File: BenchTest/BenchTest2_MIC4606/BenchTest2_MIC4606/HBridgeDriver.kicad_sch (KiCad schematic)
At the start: 39 parts, among them J1 Conn_01x01_Socket, J2 Conn_01x01_Socket, J3 Conn_01x01_Socket, J4 Conn_01x01_Socket, J5 Conn_01x01_Socket, J6 Conn_01x01_Socket, J7 Conn_01x01_Socket, J8 Conn_01x01_Socket

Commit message: WIP New Motor Design
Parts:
- removed C1: 0.1u, Capacitor_SMD:C_0402_1005Metric_Pad0.74x0.62mm_HandSolder, symbol Device:C
- removed C2: 1u, Capacitor_SMD:C_0603_1608Metric_Pad1.08x0.95mm_HandSolder, symbol Device:C
- removed C3: 2.2u, Capacitor_SMD:C_0603_1608Metric_Pad1.08x0.95mm_HandSolder, symbol Device:C
- removed C4, C5, C8, C9: 4.7n, Capacitor_SMD:C_0805_2012Metric_Pad1.18x1.45mm_HandSolder, symbol Device:C
- removed C6, C7: 10u, Capacitor_SMD:C_0805_2012Metric_Pad1.18x1.45mm_HandSolder, symbol Device:C
- removed D1, D2, D3, D4, D5, D6: D, Diode_SMD:D_SOD-123F, symbol Device:D
- removed J1, J2, J3, J4, J5, J6, J7, J8: Conn_01x01_Socket, Connector_PinHeader_2.54mm:PinHeader_1x01_P2.54mm_Vertical, symbol Connector:Conn_01x01_Socket
- removed R1: 100k, Resistor_SMD:R_0402_1005Metric_Pad0.72x0.64mm_HandSolder, symbol Device:R
- removed R10, R2, R5, R9: 6.8, Resistor_SMD:R_0805_2012Metric_Pad1.20x1.40mm_HandSolder, symbol Device:R
- removed R11, R3, R4, R8: 18, Resistor_SMD:R_0805_2012Metric_Pad1.20x1.40mm_HandSolder, symbol Device:R
- removed R6, R7: 3.3, Resistor_SMD:R_0805_2012Metric_Pad1.20x1.40mm_HandSolder, symbol Device:R
- removed TP1, TP2, TP3, TP4: TestPoint, TestPoint:TestPoint_Pad_1.0x1.0mm, symbol Connector:TestPoint
- removed U1: ~, Package_SO:TSSOP-16_4.4x5mm_P0.65mm, symbol New_Library:MIC4606

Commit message: H Bridge Continuation
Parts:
- added C1, C2, C3, C8: 0.1u, Capacitor_SMD:C_0402_1005Metric_Pad0.74x0.62mm_HandSolder, symbol Device:C
- added C10, C11, C14, C15, C16, C17, C18, C19, C9: C, symbol Device:C
- added D10, D7, D8, D9: D_Schottky, symbol Device:D_Schottky
- added D11: D, symbol Device:D
- added D12, D13: SMAJ120CA, Diode_SMD:D_SMA, symbol Diode:SMAJ120CA
- added J5, J6: Conn_01x01_Socket, symbol Connector:Conn_01x01_Socket
- added Q5, Q6: Q_NMOS_DGS, symbol Transistor_FET:Q_NMOS_DGS
- added Q7, Q8: Q_PMOS_DGS, symbol Transistor_FET:Q_PMOS_DGS
- added R10, R11, R13, R9: 33, Resistor_SMD:R_0402_1005Metric_Pad0.72x0.64mm_HandSolder, symbol Device:R
- added R15, R16, R18, R19, R20, R21, R22, R23: R, symbol Device:R
- added R17: 0, symbol Device:R
- added U10, U3: ~, Package_SO:SOIC-8_3.9x4.9mm_P1.27mm, symbol New_Library:FAN3217
- added U6, U7, U8, U9: TLP2767, Package_SO:SO-6L_10x3.84mm_P1.27mm, symbol Isolator:TLP2767
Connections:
- new net: R20.2, U8.1 (A)
- new net: D10.2 (A), Q6.2 (G), R13.2
- new net: D9.2 (A), Q8.2 (G), R11.2
- new net: R18.2, U7.1 (A)
- new net: D8.2 (A), Q7.2 (G), R10.2
- new net: R15.2, U6.1 (A)
- new net: D7.2 (A), Q5.2 (G), R9.2
- new net: R21.2, U9.1 (A)
- new net F1: D12.2 (A2), J5.1 (Pin_1), Q5.1 (D), Q7.3 (S)
- new net F2: D13.2 (A2), J6.1 (Pin_1), Q6.1 (D), Q8.3 (S)
- new net G+_1: D8.1 (K), R10.1, U3.7 (OUTA)
- new net G+_2: D9.1 (K), R11.1, U10.7 (OUTA)
- new net G-_1: D7.1 (K), R9.1, U3.5 (OUTB)
- new net G-_2: D10.1 (K), R13.1, U10.5 (OUTB)
- new net GND: C1.2, C2.2, C3.2, C8.2, U10.3 (GND), U3.3 (GND), U6.3 (K), U6.4 (GND), U7.3 (K), U7.4 (GND), U8.3 (K), U8.4 (GND), U9.3 (K), U9.4 (GND)
- new net IN1+: R15.1, R16.1
- new net IN1-: R18.1, R19.1
- new net IN2+: R20.1, R23.1
- new net IN2-: R21.1, R22.1
- new net INA1: R16.2, U10.2 (INA), U3.2 (INA), U6.5 (VO), U8.5 (VO)
- new net INA2: R23.2
- new net INB1: R19.2, U3.4 (INB), U7.5 (VO)
- new net INB2: R22.2, U10.4 (INB), U9.5 (VO)
- new net VBAT+: C10.1, C11.1, C14.1, C15.1, C16.1, C17.1, C18.1, C19.1, C9.1, Q7.1 (D), Q8.1 (D)
- new net VBAT-: C10.2, C11.2, C14.2, C15.2, C16.2, C17.2, C18.2, C19.2, C9.2, D12.1 (A1), D13.1 (A1), Q5.3 (S), Q6.3 (S)
- new net Vdrive: D11.2 (A), R17.1
- new net Vdrive_iso: C1.1, C2.1, C3.1, C8.1, D11.1 (K), R17.2, U10.6 (VDD), U3.6 (VDD), U6.6 (VDD), U7.6 (VDD), U8.6 (VDD), U9.6 (VDD)
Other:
- note added: "Cap Bank Effective Capacitance: TODO"
- note added: "TODO investigate this"
- note added: "TODO why TVS? TODO What voltage? > vbat?"

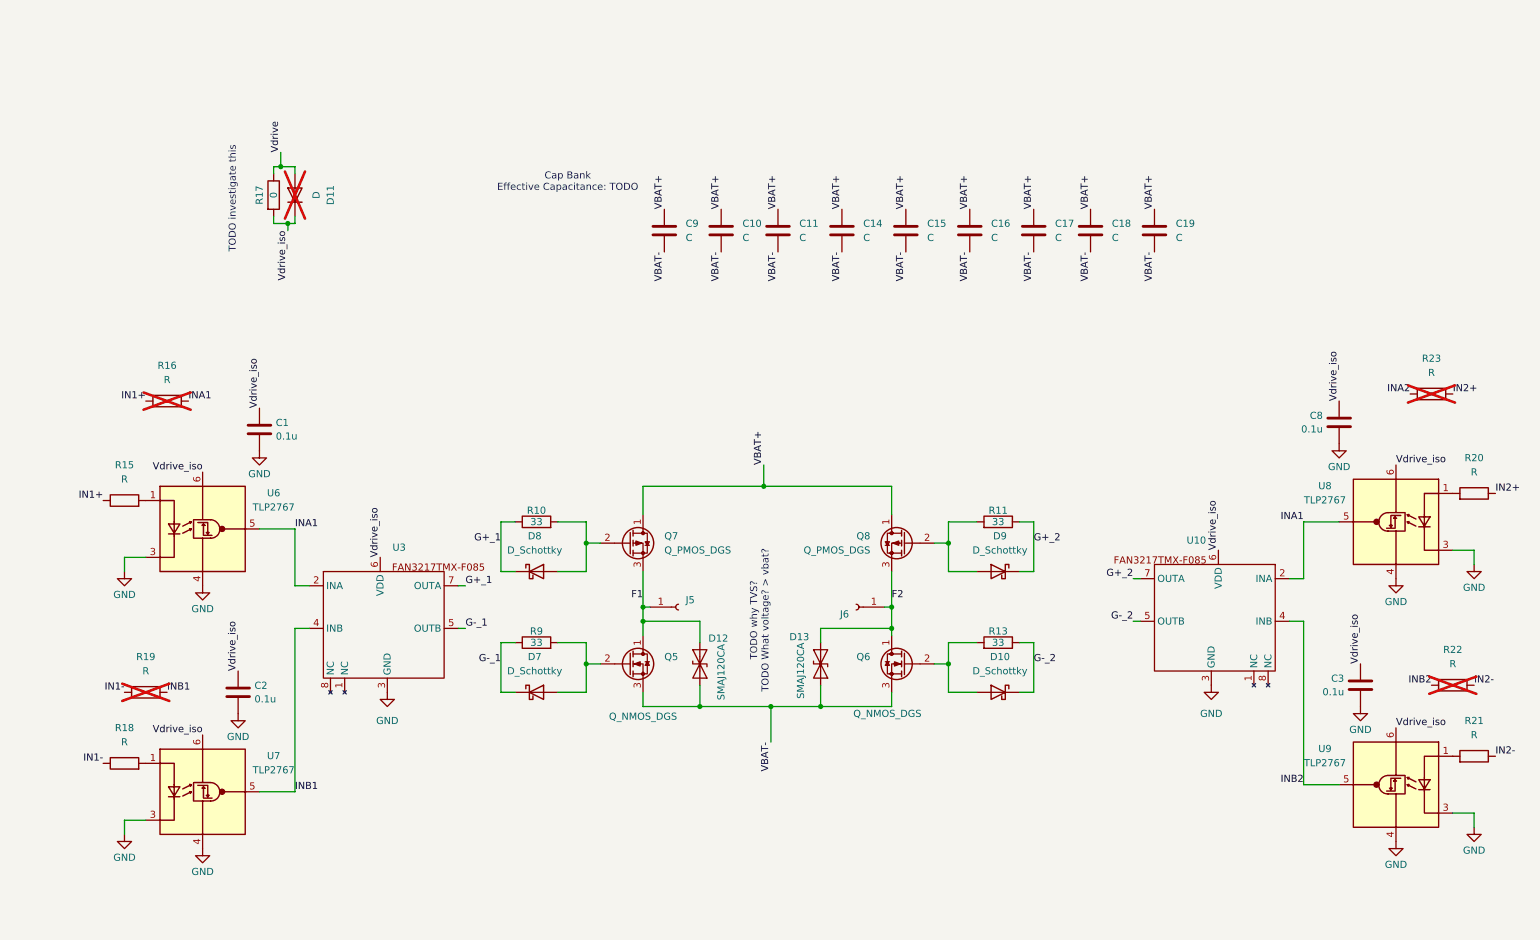
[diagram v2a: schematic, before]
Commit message: Defined Some parts, added notes for Arm/regen/H bridge
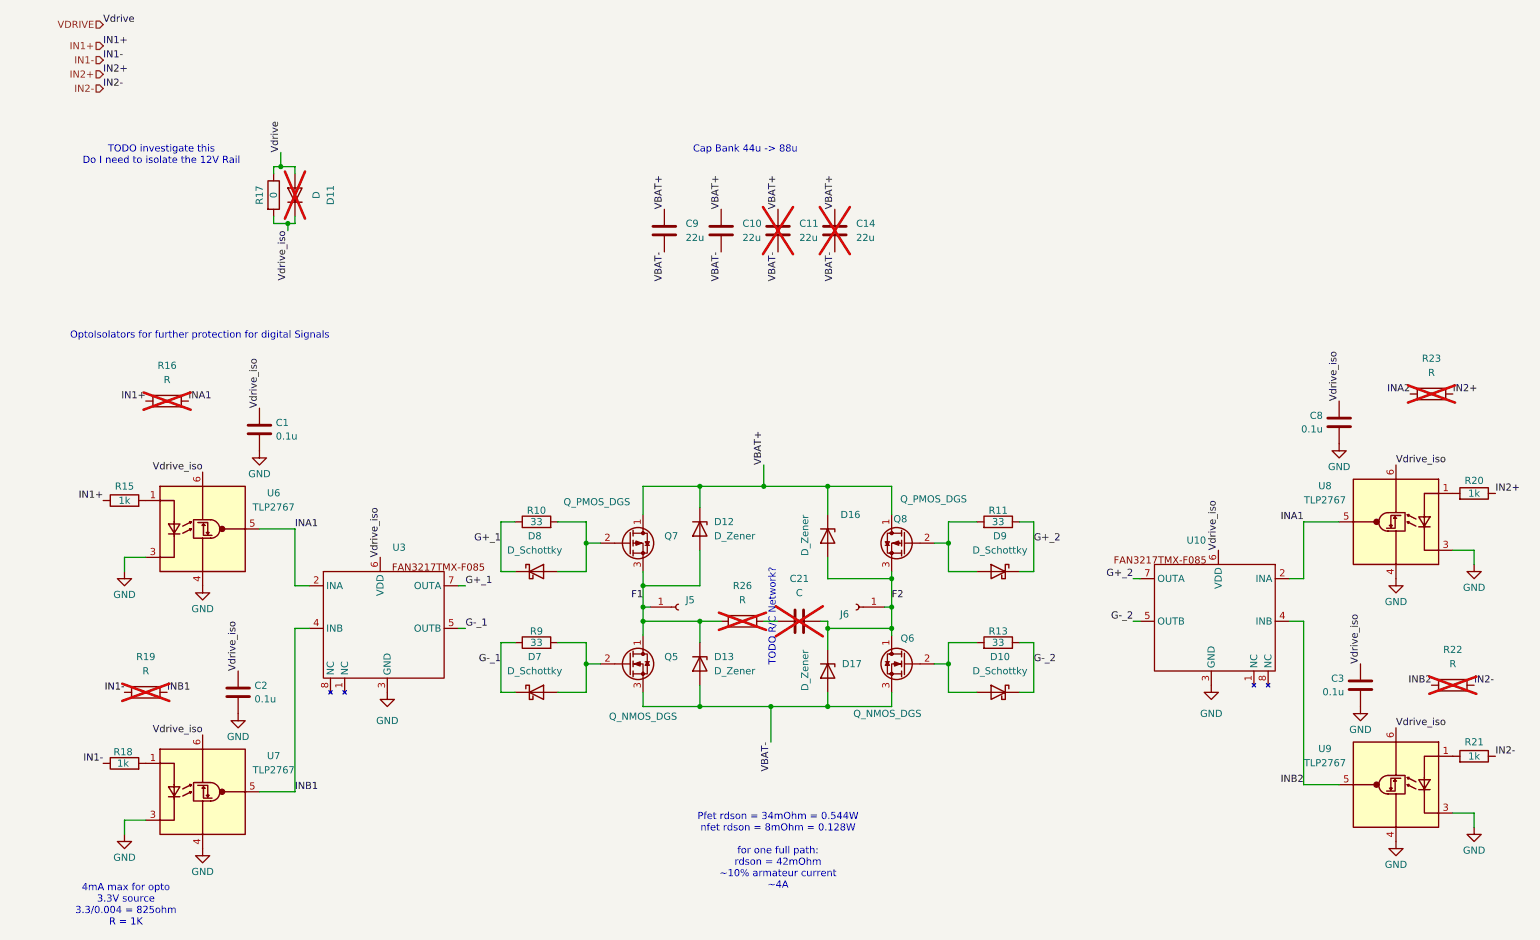
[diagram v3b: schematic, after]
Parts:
- removed C15, C16, C17, C18, C19: C, symbol Device:C
- removed D12, D13: SMAJ120CA, Diode_SMD:D_SMA, symbol Diode:SMAJ120CA
- added C21: C, Capacitor_SMD:C_1206_3216Metric_Pad1.33x1.80mm_HandSolder, symbol Device:C
- added D12, D13, D16, D17: D_Zener, Diode_SMD:D_SMC, symbol Device:D_Zener
- added R26: R, Resistor_SMD:R_1206_3216Metric_Pad1.30x1.75mm_HandSolder, symbol Device:R
- C10, C9: value C -> 22u; P/N (none) -> 226AVG100MFBJ
- C11, C14: value C -> 22u; P/N (none) -> 226AVG100MFBJ; now not fitted
- R15, R18, R20, R21: value R -> 1k
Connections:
- net F1: now also D12.2 (A), D13.1 (K), R26.1
- net F2: now also C21.2, D16.2 (A), D17.1 (K)
- net VBAT+: now also D12.1 (K), D16.1 (K)
- net VBAT-: now also D13.2 (A), D17.2 (A)
- net Vdrive renamed VDRIVE
- new net: C21.1, R26.2
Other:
- note added: "4mA max for opto 3.3V source 3.3/0.004 = 825ohm R = 1K"
- note added: "Cap Bank 44u -> 88u"
- note added: "OptoIsolators for further protection for digital Signals"
- note added: "Pfet rdson = 34mOhm = 0.544W nfet rdson = 8mOhm = 0.128W for one full path: rdson = 42mOhm ~10% armateur current ~4A"
- note added: "TODO R/C Network?"
- note added: "TODO investigate this Do I need to isolate the 12V Rail"
- note removed: "Cap Bank Effective Capacitance: TODO"
- note removed: "TODO investigate this"
- note removed: "TODO why TVS? TODO What voltage? > vbat?"

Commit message: Additional Documents / Routing
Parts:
- removed J5, J6: Conn_01x01_Socket, symbol Connector:Conn_01x01_Socket
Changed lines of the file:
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@@
 		)
 	)
-	(label "F1"
-		(at 118.11 119.38 180)
-		(effects
-			(font
-				(size 1.27 1.27)
-			)
-			(justify right bottom)
-		)
-	)
 	(label "IN1+"
 		(at 21.59 101.6 180)
@@
 		)
 	)
+	(label "F1"
+		(at 21.59 33.02 0)
+		(effects
+			(font
+				(size 1.27 1.27)
+			)
+			(justify left bottom)
+		)
+	)
 	(label "INB1"
 		(at 55.88 153.67 0)
@@
 		)
 	)
+	(label "F2"
+		(at 161.29 120.65 180)
+		(effects
+			(font
+				(size 1.27 1.27)
+			)
+			(justify right bottom)
+		)
+	)
 	(label "VBAT+"
 		(at 121.92 49.53 90)
@@
 		)
 	)
+	(label "F2"
+		(at 21.59 35.56 0)
+		(effects
+			(font
+				(size 1.27 1.27)
+			)
+			(justify left bottom)
+		)
+	)
 	(label "VBAT-"
 		(at 140.97 144.78 270)
@@
 		)
 	)
-	(label "F2"
-		(at 162.56 119.38 0)
-		(effects
-			(font
-				(size 1.27 1.27)
-			)
-			(justify left bottom)
-		)
-	)
 	(label "G-_2"
 		(at 187.96 130.81 0)
@@
 		)
 	)
+	(label "F1"
+		(at 119.38 120.65 0)
+		(effects
+			(font
+				(size 1.27 1.27)
+			)
+			(justify left bottom)
+		)
+	)
 	(hierarchical_label "IN1+"
 		(shape input)
@@
 		)
 	)
+	(hierarchical_label "F2"
+		(shape input)
+		(at 21.59 35.56 180)
+		(effects
+			(font
+				(size 1.27 1.27)
+			)
+			(justify right)
+		)
+	)
+	(hierarchical_label "F1"
+		(shape input)
+		(at 21.59 33.02 180)
+		(effects
+			(font
+				(size 1.27 1.27)
+			)
+			(justify right)
+		)
+	)
 	(hierarchical_label "IN2+"
 		(shape input)
@@
 	)
 	(symbol
-		(lib_id "Connector:Conn_01x01_Socket")
-		(at 156.21 120.65 180)
-		(unit 1)
-		(exclude_from_sim no)
-		(in_bom yes)
-		(on_board yes)
-		(dnp no)
-		(property "Reference" "J6"
-			(at 154.94 121.9201 0)
-			(effects
-				(font
-					(size 1.27 1.27)
-				)
-				(justify left)
-			)
-		)
-		(property "Value" "Conn_01x01_Socket"
-			(at 159.766 117.094 0)
-			(effects
-				(font
-					(size 1.27 1.27)
-				)
-				(justify left)
-				(hide yes)
-			)
-		)
-		(property "Footprint" ""
-			(at 156.21 120.65 0)
-			(effects
-				(font
-					(size 1.27 1.27)
-				)
-				(hide yes)
-			)
-		)
-		(property "Datasheet" "~"
-			(at 156.21 120.65 0)
-			(effects
-				(font
-					(size 1.27 1.27)
-				)
-				(hide yes)
-			)
-		)
-		(property "Description" "Generic connector, single row, 01x01, script generated"
-			(at 156.21 120.65 0)
-			(effects
-				(font
-					(size 1.27 1.27)
-				)
-				(hide yes)
-			)
-		)
-		(pin "1"
-		)
-		(instances
-			(project "BenchTest2_MIC4606"
-				(path "/5c5197d3-4aa5-4f8b-b790-1e4b8d49fd62/ca249708-ec09-41b0-b71d-70bebe19cbfd"
-					(reference "J6")
-					(unit 1)
-				)
-			)
-		)
-	)
-	(symbol
 		(lib_id "Device:C")
 		(at 132.08 53.34 0)
@@
 					(unit 1)
 				)
-			)
-		)
-	)
-	(symbol
-		(lib_id "Connector:Conn_01x01_Socket")
-		(at 124.46 120.65 0)
-		(unit 1)
-		(exclude_from_sim no)
-		(in_bom yes)
-		(on_board yes)
-		(dnp no)
-		(property "Reference" "J5"
-			(at 125.73 119.3799 0)
-			(effects
-				(font
-					(size 1.27 1.27)
-				)
-				(justify left)
-			)
-		)
-		(property "Value" "Conn_01x01_Socket"
-			(at 120.904 124.206 0)
-			(effects
-				(font
-					(size 1.27 1.27)
-				)
-				(justify left)
-				(hide yes)
-			)
-		)
-		(property "Footprint" ""
-			(at 124.46 120.65 0)
-			(effects
-				(font
-					(size 1.27 1.27)
-				)
-				(hide yes)
-			)
-		)
-		(property "Datasheet" "~"
-			(at 124.46 120.65 0)
-			(effects
-				(font
-					(size 1.27 1.27)
-				)
-				(hide yes)
-			)
-		)
-		(property "Description" "Generic connector, single row, 01x01, script generated"
-			(at 124.46 120.65 0)
-			(effects
-				(font
-					(size 1.27 1.27)
-				)
-				(hide yes)
-			)
-		)
-		(pin "1"
-		)
-		(instances
-			(project ""
-				(path "/5c5197d3-4aa5-4f8b-b790-1e4b8d49fd62/ca249708-ec09-41b0-b71d-70bebe19cbfd"
-					(reference "J5")
-					(unit 1)
-				)

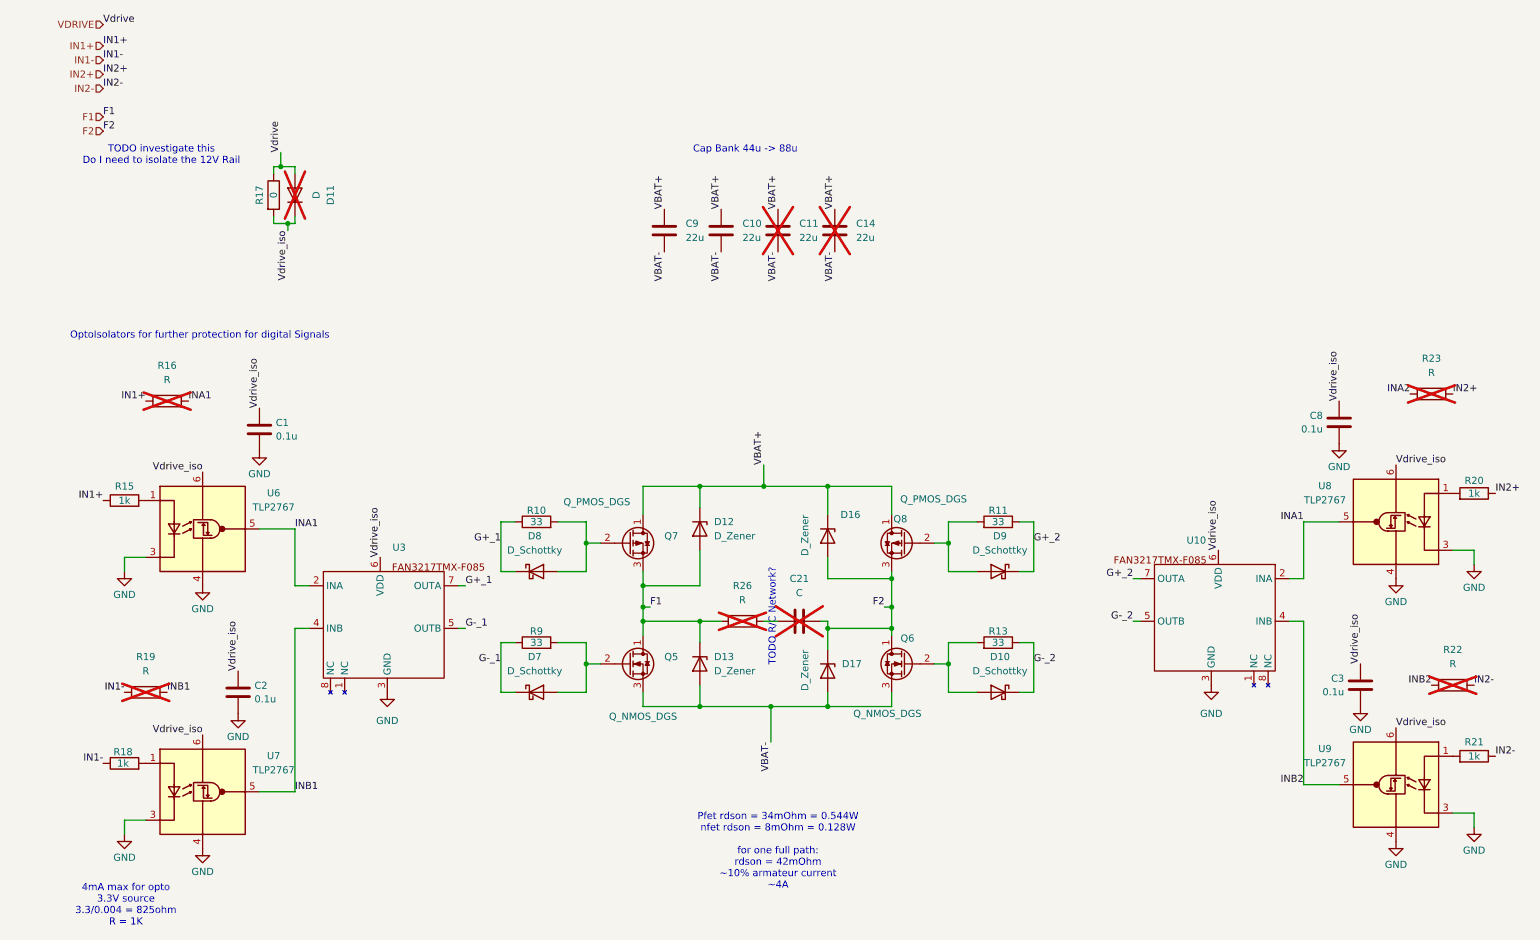
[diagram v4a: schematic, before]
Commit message: Removed Optoisolators from digital Signals
Will be requiring these on the drive side
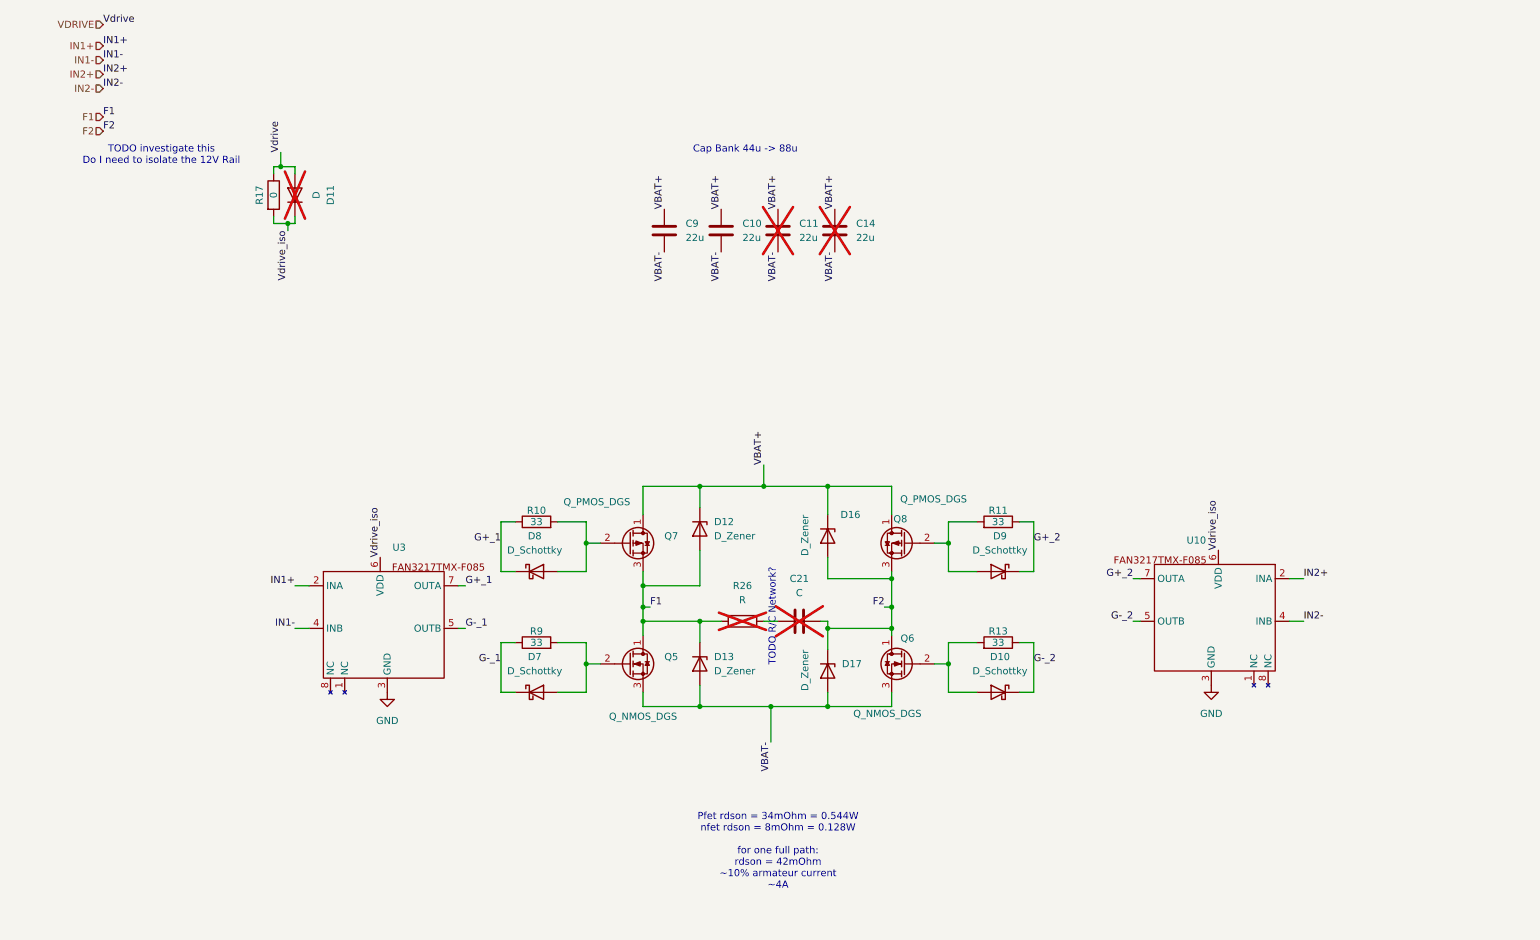
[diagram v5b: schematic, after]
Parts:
- removed C1, C2, C3, C8: 0.1u, Capacitor_SMD:C_0402_1005Metric_Pad0.74x0.62mm_HandSolder, symbol Device:C
- removed R15, R18, R20, R21: 1k, symbol Device:R
- removed R16, R19, R22, R23: R, symbol Device:R
- removed U6, U7, U8, U9: TLP2767, Package_SO:SO-6L_10x3.84mm_P1.27mm, symbol Isolator:TLP2767
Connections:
- net INB1 is gone; now on net IN1-: U3.4 (INB)
- net INB2 is gone; now on net IN2-: U10.4 (INB)
- net IN1+: now also U3.2 (INA)
- net IN2+: now also U10.2 (INA)
- removed net INA1: U10.2 (INA), U3.2 (INA)
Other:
- note removed: "4mA max for opto 3.3V source 3.3/0.004 = 825ohm R = 1K"
- note removed: "OptoIsolators for further protection for digital Signals"
